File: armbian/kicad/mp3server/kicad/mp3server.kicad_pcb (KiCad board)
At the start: 2 copper layers, 101.6 x 76.2 mm, 29 parts, among them J1 Conn_01x02, J2 USB_2, P1 CONN_1, P10 CONN_1, P11 CONN_1, P12 CONN_1, P13 CONN_1, P14 CONN_1, P15 CONN_1, P16 CONN_1, P17 CONN_1, P18 CONN_1, P19 CONN_1, P2 CONN_1, P3 ROCKPI_S, P4 CONN_5, P5 CONN_5, P6 CONN_3, P7 CONN_4X1, P8 ROCKPI_S_H2

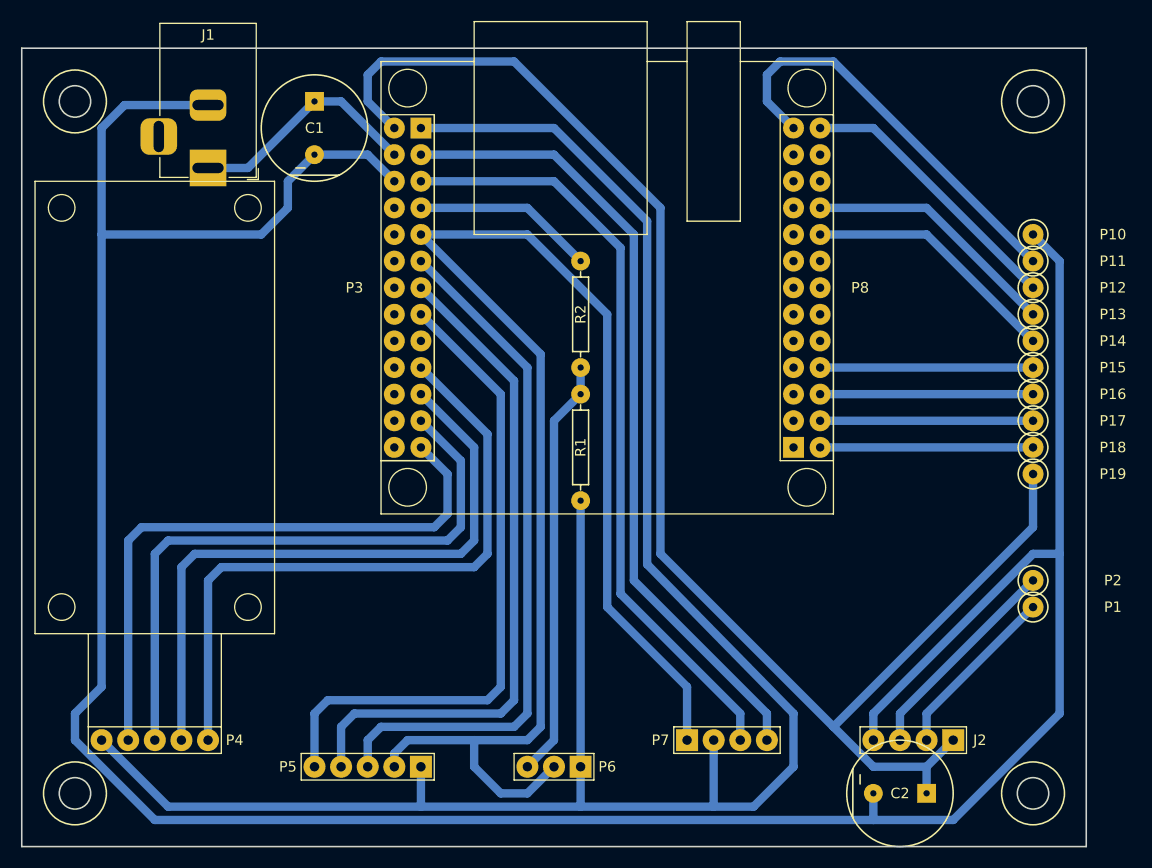
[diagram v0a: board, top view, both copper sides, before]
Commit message: mp3server: the pcb accepts orangepi zero or rockpis
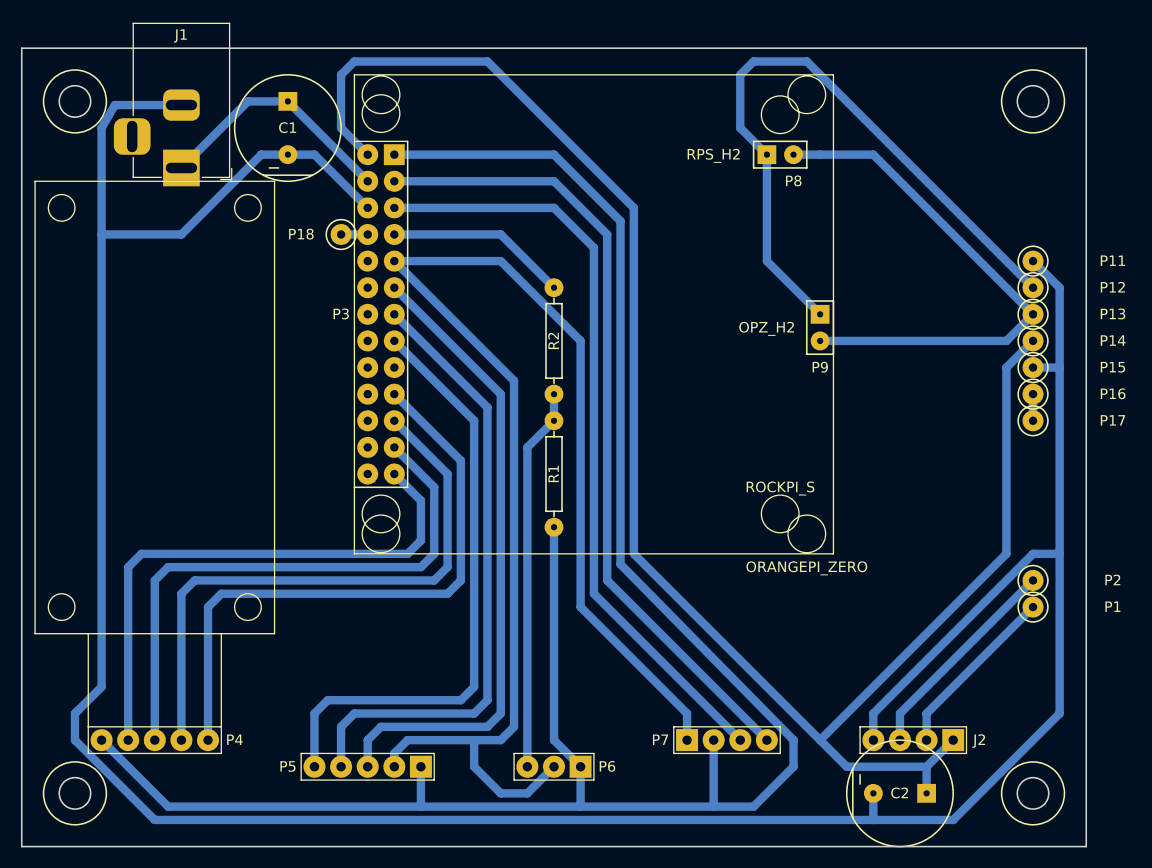
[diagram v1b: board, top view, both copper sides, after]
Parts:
- removed P10, P19: CONN_1, kicad:PIN_ARRAY_1X1
- added P9: CONN_2, kicad:PIN_ARRAY_2X1, F.Cu at (121.9, 110.5)
- P3: footprint kicad:ROCKPI_S -> kicad:RPS_OPZ
- P8: value ROCKPI_S_H2 -> CONN_2; footprint kicad:PIN_ARRAY_13X2 -> kicad:PIN_ARRAY_2X1
- moved P18 69.1 mm to (76.2, 101.6)
- moved P8 13.0 mm to (118.1, 94.0), turned to 0 degrees
- moved R2 3.59 mm to (96.5, 111.8)
- moved R1 3.59 mm to (96.5, 124.5)
- moved P3 3.59 mm to (99.1, 109.2)
- moved J1 2.54 mm to (61.0, 95.2)
- moved C1 2.54 mm to (71.1, 91.4)
- turned P11 to 0 degrees
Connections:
- P11 pad 1: Net-(P11-Pad1) -> Net-(C1-Pad2)
- P14 pad 1: Net-(P14-Pad1) -> Net-(C2-Pad1)
- P15 pad 1: Net-(P15-Pad1) -> Net-(C1-Pad2)
- P17 pad 1: Net-(P17-Pad1) -> Net-(P16-Pad1)
- P3 pad 8: (no net) -> Net-(P18-Pad1)
- P8 pad 1: (no net) -> Net-(P12-Pad1)
- P8 pad 2: Net-(P18-Pad1) -> Net-(P13-Pad1)
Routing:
- net Net-(P11-Pad1): track 39.9 -> 0.00 mm
- net Net-(P12-Pad1): track 26.6 -> 63.4 mm
- net Net-(P13-Pad1): track 24.5 -> 50.5 mm
- net Net-(P14-Pad1): track 24.5 -> 0.00 mm
- net Net-(P17-Pad1): track 20.3 -> 0.00 mm
- net Net-(P15-Pad1): track 20.3 -> 0.00 mm
- net Net-(C2-Pad1): track 145.4 -> 165.0 mm
- net Net-(P18-Pad1): track 20.3 -> 2.54 mm
- net Net-(P16-Pad1): track 20.3 -> 2.54 mm
- net Net-(P3-Pad9): track 145.0 -> 138.4 mm
- net Net-(C1-Pad2): track 281.5 -> 276.3 mm
- net Net-(P3-Pad25): track 58.0 -> 52.9 mm
- net Net-(P3-Pad19): track 63.4 -> 58.3 mm
- net Net-(P3-Pad21): track 61.6 -> 56.5 mm
- net Net-(P3-Pad11): track 66.2 -> 61.1 mm
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
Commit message: mp3server: revert last pcb changes for orange pi zero (not in the same direction)
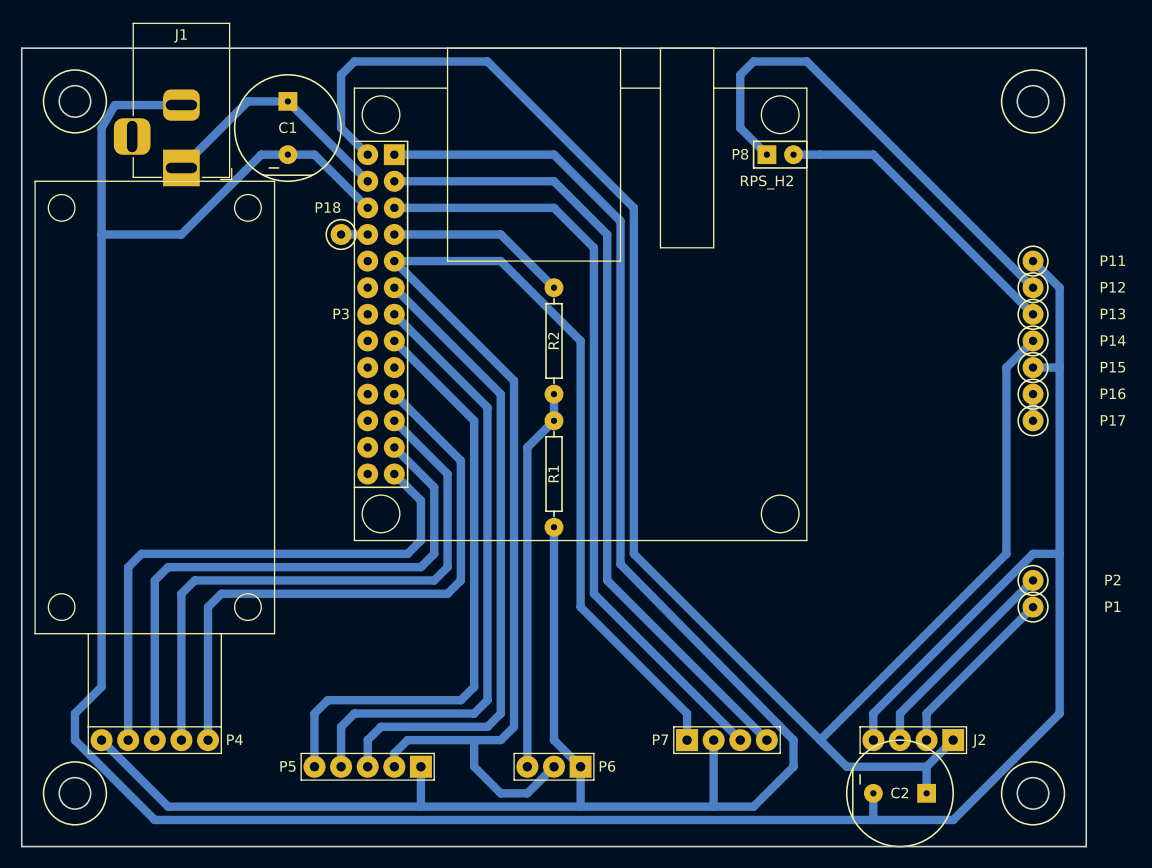
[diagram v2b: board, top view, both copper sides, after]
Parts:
- removed P9: CONN_2, kicad:PIN_ARRAY_2X1
- P3: footprint kicad:RPS_OPZ -> kicad:ROCKPI_S
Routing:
- net Net-(P13-Pad1): track 50.5 -> 29.2 mm
- net Net-(P12-Pad1): track 63.4 -> 46.1 mm

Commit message: add armbian/kicad/remoteControl
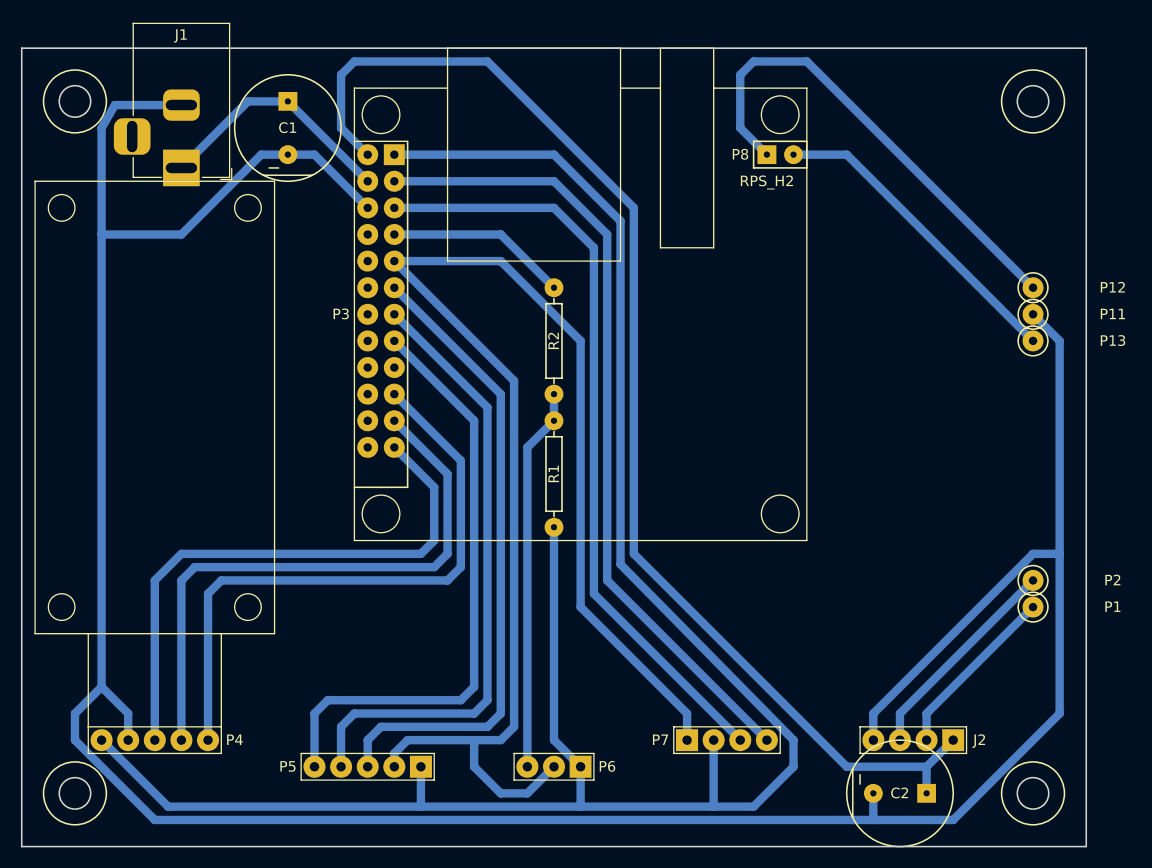
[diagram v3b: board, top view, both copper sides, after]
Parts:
- removed P14, P15, P16, P17, P18: CONN_1, kicad:PIN_ARRAY_1X1
- P3: value ROCKPI_S -> PI
- moved P11 5.08 mm to (142.2, 109.2)
- moved P13 2.54 mm to (142.2, 111.8)
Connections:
- P3 pad 8: Net-(P18-Pad1) -> (no net)
- P4 pad 2: Net-(P3-Pad25) -> Net-(C1-Pad2)
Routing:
- net Net-(P3-Pad25): track 52.9 -> 0.00 mm
- net Net-(C2-Pad1): track 165.0 -> 118.4 mm
- net Net-(P18-Pad1): track 2.54 -> 0.00 mm
- net Net-(P16-Pad1): track 2.54 -> 0.00 mm
- net Net-(C1-Pad2): track 276.3 -> 274.8 mm
- net Net-(P13-Pad1): track 29.2 -> 30.2 mm
- net Net-(P3-Pad23): track 54.7 -> 54.0 mm
